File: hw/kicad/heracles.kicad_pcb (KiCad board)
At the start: 2 copper layers, 61 parts, among them J1 USB-MICRO, K1 MOTOR_CONV, P1 LOGIC_BAT, P2 MOTOR_BAT, P3 MOTOR_A, P4 MOTOR_B, P5 CONN_8, P6 CONN_8, P7 CONN_8, P8 CONN_8, P9 CONN_8, Q1 FDV301N, Q2 FDV304P, SW1 B3U-1000P, SW2 B3U-1000P, T1 TPS62056, T2 LM3480, U1 TB6612FNG, U2 HC-05, U3 LY330ALH, U4 MMA6341L, U5 STM32F103CBT6

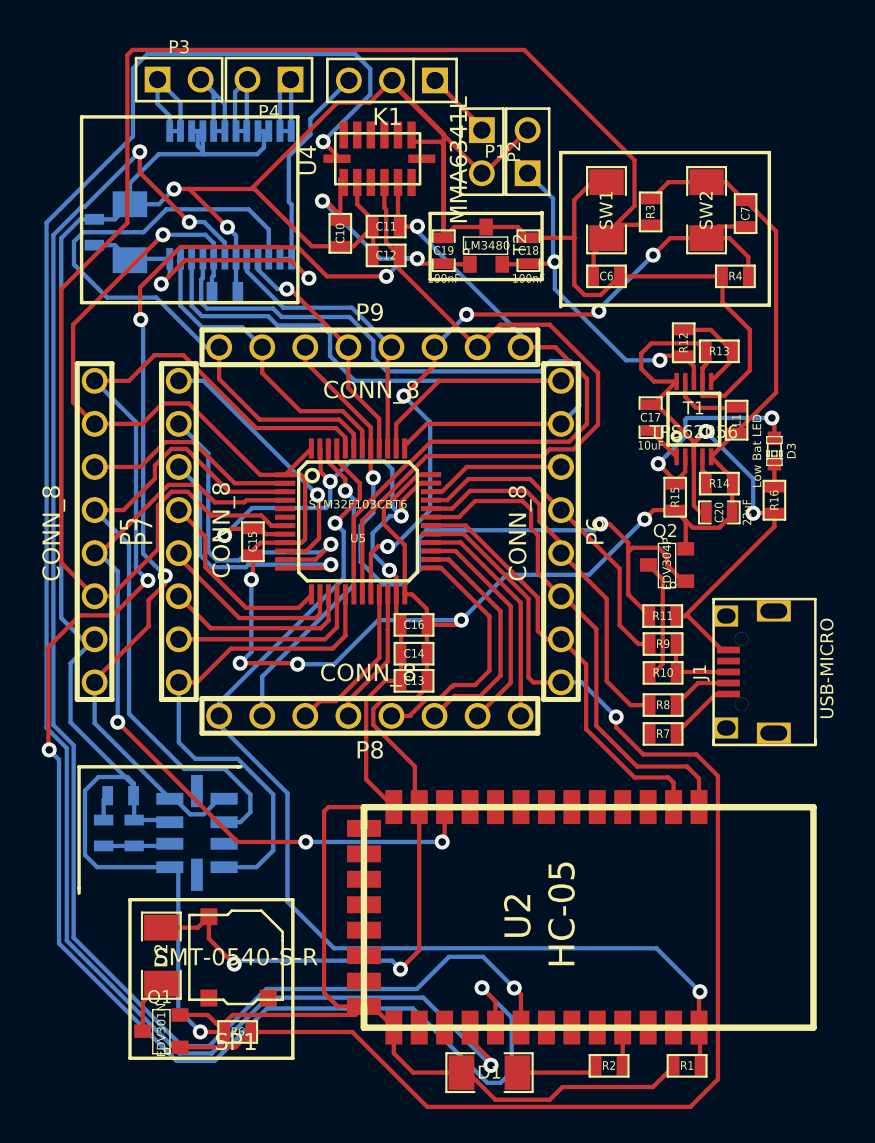
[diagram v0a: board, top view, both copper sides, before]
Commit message: Added some missing connections in pcb
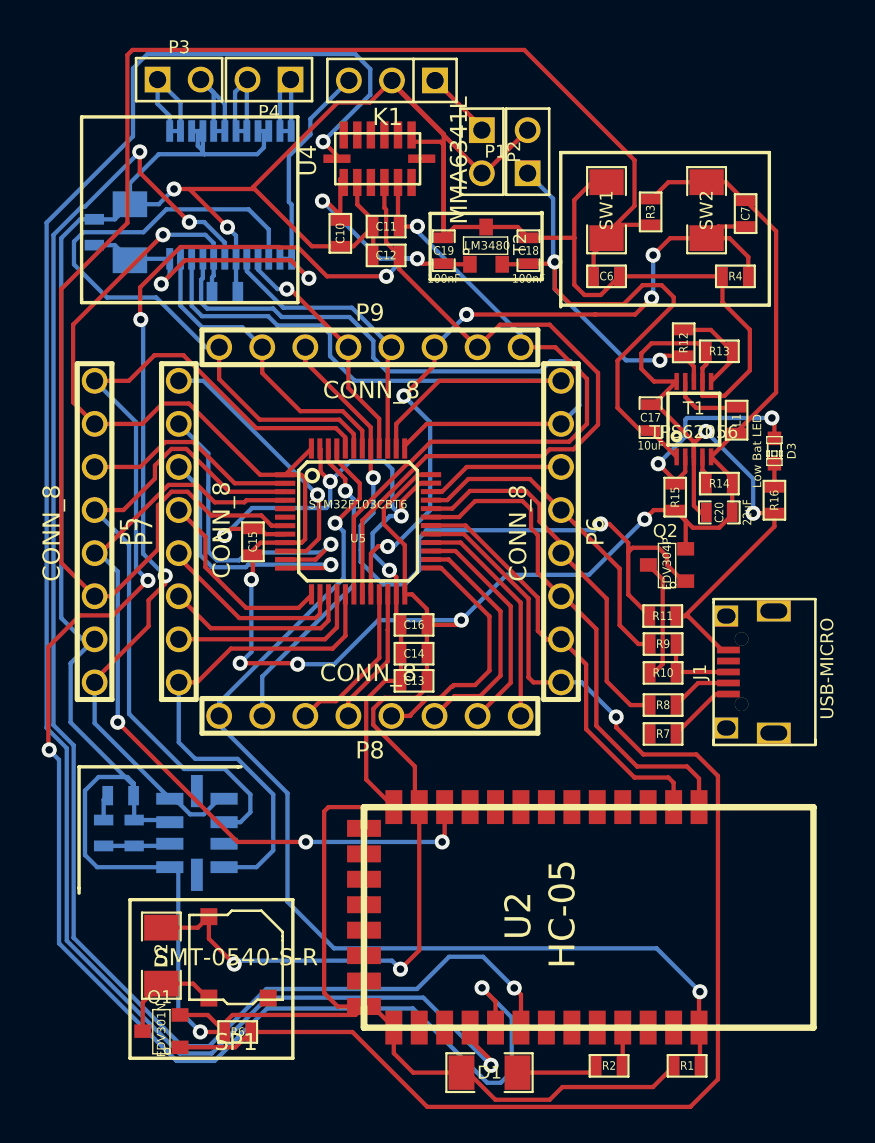
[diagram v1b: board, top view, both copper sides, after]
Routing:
- net /Power/VIN: track 24.4 -> 44.5 mm
- net N-0000086: track 3.25 -> 6.41 mm
- net /Microcontroller/PB2-BOOT1: track 43.4 -> 44.8 mm
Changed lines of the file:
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@@
   (general
     (links 181)
-    (no_connects 2)
+    (no_connects 0)
     (area 195.601 157.2338 243.0625 220.547001)
     (thickness 1.6)
     (drawings 27)
-    (tracks 937)
+    (tracks 953)
     (zones 0)
     (modules 61)
@@
   (segment (start 224.29 190.69) (end 224.29 197.37) (width 0.254) (layer F.Cu) (net 30))
   (segment (start 220.7446 187.1446) (end 224.29 190.69) (width 0.254) (layer F.Cu) (net 30))
+  (segment (start 228.67 173.7) (end 231.04 173.7) (width 0.254) (layer F.Cu) (net 31))
+  (segment (start 233.099 169.201) (end 232.1 170.2) (width 0.254) (layer F.Cu) (net 31))
+  (via (at 232.1 170.2) (size 0.889) (layers F.Cu B.Cu) (net 31))
+  (segment (start 233.099 169.201) (end 235.25 169.201) (width 0.254) (layer F.Cu) (net 31))
+  (segment (start 232.1 172.64) (end 232.1 170.2) (width 0.254) (layer B.Cu) (net 31))
+  (segment (start 232.01 172.73) (end 232.1 172.64) (width 0.254) (layer B.Cu) (net 31))
+  (via (at 232.01 172.73) (size 0.889) (layers F.Cu B.Cu) (net 31))
+  (segment (start 231.04 173.7) (end 232.01 172.73) (width 0.254) (layer F.Cu) (net 31))
   (segment (start 215.89 187.36) (end 216.43 187.36) (width 0.254) (layer F.Cu) (net 31))
   (segment (start 216.84 187.35) (end 218.95 185.24) (width 0.254) (layer B.Cu) (net 31))
@@
   (segment (start 215.9 187.35) (end 215.89 187.36) (width 0.254) (layer F.Cu) (net 31))
   (segment (start 215.89 187.36) (end 215.45692 187.79308) (width 0.254) (layer F.Cu) (net 31))
-  (segment (start 235.25 169.201) (end 233.099 169.201) (width 0.254) (layer F.Cu) (net 31))
   (segment (start 219.21 175.59) (end 219.21 175.63) (width 0.254) (layer B.Cu) (net 31))
   (segment (start 221.1 173.7) (end 219.21 175.59) (width 0.254) (layer B.Cu) (net 31))
   (via (at 221.1 173.7) (size 0.889) (layers F.Cu B.Cu) (net 31))
-  (segment (start 228.7 173.7) (end 221.1 173.7) (width 0.254) (layer F.Cu) (net 31))
-  (segment (start 228.9 173.5) (end 228.7 173.7) (width 0.254) (layer F.Cu) (net 31))
-  (via (at 228.9 173.5) (size 0.889) (layers F.Cu B.Cu) (net 31))
-  (segment (start 228.9 173.4) (end 228.9 173.5) (width 0.254) (layer B.Cu) (net 31))
-  (segment (start 232.1 170.2) (end 228.9 173.4) (width 0.254) (layer B.Cu) (net 31))
-  (via (at 232.1 170.2) (size 0.889) (layers F.Cu B.Cu) (net 31))
-  (segment (start 233.099 169.201) (end 232.1 170.2) (width 0.254) (layer F.Cu) (net 31))
+  (segment (start 228.7 173.7) (end 228.67 173.7) (width 0.254) (layer F.Cu) (net 31))
+  (segment (start 228.67 173.7) (end 221.1 173.7) (width 0.254) (layer F.Cu) (net 31))
   (segment (start 235.25 169.201) (end 236.601 169.201) (width 0.254) (layer F.Cu) (net 31))
-  (segment (start 237.712 170.312) (end 237.712 171.45) (width 0.254) (layer F.Cu) (net 31))
   (segment (start 236.601 169.201) (end 237.712 170.312) (width 0.254) (layer F.Cu) (net 31))
+  (segment (start 237.712 170.312) (end 237.712 171.45) (width 0.254) (layer F.Cu) (net 31))
   (segment (start 237.55 168.512) (end 235.939 168.512) (width 0.254) (layer F.Cu) (net 31))
   (segment (start 235.939 168.512) (end 235.25 169.201) (width 0.254) (layer F.Cu) (net 31))
@@
   (segment (start 235.008 182.878) (end 235.008 182.0925) (width 0.254) (layer F.Cu) (net 49))
   (segment (start 235.238 183.108) (end 235.008 182.878) (width 0.254) (layer F.Cu) (net 49))
+  (segment (start 231.95 180.542) (end 231.342 180.542) (width 0.254) (layer F.Cu) (net 50) (status 400000))
+  (segment (start 226.3 172.18) (end 226.3 170.6) (width 0.254) (layer F.Cu) (net 50))
+  (segment (start 227.21 173.09) (end 226.3 172.18) (width 0.254) (layer F.Cu) (net 50))
+  (segment (start 230.36 173.09) (end 227.21 173.09) (width 0.254) (layer F.Cu) (net 50))
+  (segment (start 231.48 171.97) (end 230.36 173.09) (width 0.254) (layer F.Cu) (net 50))
+  (segment (start 232.6 171.97) (end 231.48 171.97) (width 0.254) (layer F.Cu) (net 50))
+  (segment (start 233.31 172.68) (end 232.6 171.97) (width 0.254) (layer F.Cu) (net 50))
+  (segment (start 233.31 173.11) (end 233.31 172.68) (width 0.254) (layer F.Cu) (net 50))
+  (segment (start 230 176.42) (end 233.31 173.11) (width 0.254) (layer F.Cu) (net 50))
+  (segment (start 230 179.2) (end 230 176.42) (width 0.254) (layer F.Cu) (net 50))
+  (segment (start 231.342 180.542) (end 230 179.2) (width 0.254) (layer F.Cu) (net 50))
   (segment (start 231.95 180.542) (end 231.95 180.5585) (width 0.254) (layer F.Cu) (net 50))
   (segment (start 231.95 180.5585) (end 232.3 180.9085) (width 0.254) (layer F.Cu) (net 50))
   (segment (start 226.3 170.6) (end 226.3 172.2) (width 0.254) (layer B.Cu) (net 50))
-  (segment (start 232.768 176.132) (end 233.9 176.132) (width 0.254) (layer F.Cu) (net 50))
-  (segment (start 232.5 176.4) (end 232.768 176.132) (width 0.254) (layer F.Cu) (net 50))
-  (via (at 232.5 176.4) (size 0.889) (layers F.Cu B.Cu) (net 50))
-  (segment (start 230.5 176.4) (end 232.5 176.4) (width 0.254) (layer B.Cu) (net 50))
   (segment (start 226.3 172.2) (end 230.5 176.4) (width 0.254) (layer B.Cu) (net 50))
+  (segment (start 230.5 176.4) (end 232.5 176.4) (width 0.254) (layer B.Cu) (net 50))
+  (via (at 232.5 176.4) (size 0.889) (layers F.Cu B.Cu) (net 50))
+  (segment (start 232.5 176.4) (end 232.768 176.132) (width 0.254) (layer F.Cu) (net 50))
+  (segment (start 232.768 176.132) (end 233.9 176.132) (width 0.254) (layer F.Cu) (net 50))
   (segment (start 224.75 170.702) (end 226.198 170.702) (width 0.254) (layer F.Cu) (net 50))
+  (segment (start 226.198 170.702) (end 226.3 170.6) (width 0.254) (layer F.Cu) (net 50))
   (segment (start 226.2 166.87) (end 224.7 165.37) (width 0.254) (layer B.Cu) (net 50))
-  (segment (start 226.2 170.5) (end 226.2 166.87) (width 0.254) (layer B.Cu) (net 50))
   (segment (start 226.3 170.6) (end 226.2 170.5) (width 0.254) (layer B.Cu) (net 50))
+  (segment (start 226.2 170.5) (end 226.2 166.87) (width 0.254) (layer B.Cu) (net 50))
   (via (at 226.3 170.6) (size 0.889) (layers F.Cu B.Cu) (net 50))
-  (segment (start 226.198 170.702) (end 226.3 170.6) (width 0.254) (layer F.Cu) (net 50))
   (segment (start 223.2025 170.73982) (end 224.71218 170.73982) (width 0.254) (layer F.Cu) (net 50))
   (segment (start 224.71218 170.73982) (end 224.75 170.702) (width 0.254) (layer F.Cu) (net 50))
@@
   (segment (start 199.7 203.508) (end 199.7 202.308) (width 0.254) (layer B.Cu) (net 58))
   (segment (start 199.7 202.308) (end 199.938 202.07) (width 0.254) (layer B.Cu) (net 58))
+  (segment (start 205.904 214.004) (end 205.824 214.004) (width 0.254) (layer F.Cu) (net 59) (status C00000))
+  (segment (start 204.975 213.155) (end 203.104 213.155) (width 0.254) (layer F.Cu) (net 59) (status 800000))
+  (segment (start 205.824 214.004) (end 204.975 213.155) (width 0.254) (layer F.Cu) (net 59) (status 400000))
   (segment (start 202.00418 215.954) (end 202.00418 214.25482) (width 0.254) (layer F.Cu) (net 59))
   (segment (start 202.00418 214.25482) (end 203.104 213.155) (width 0.254) (layer F.Cu) (net 59))

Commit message: Fixed Q1 and Q2 footprints
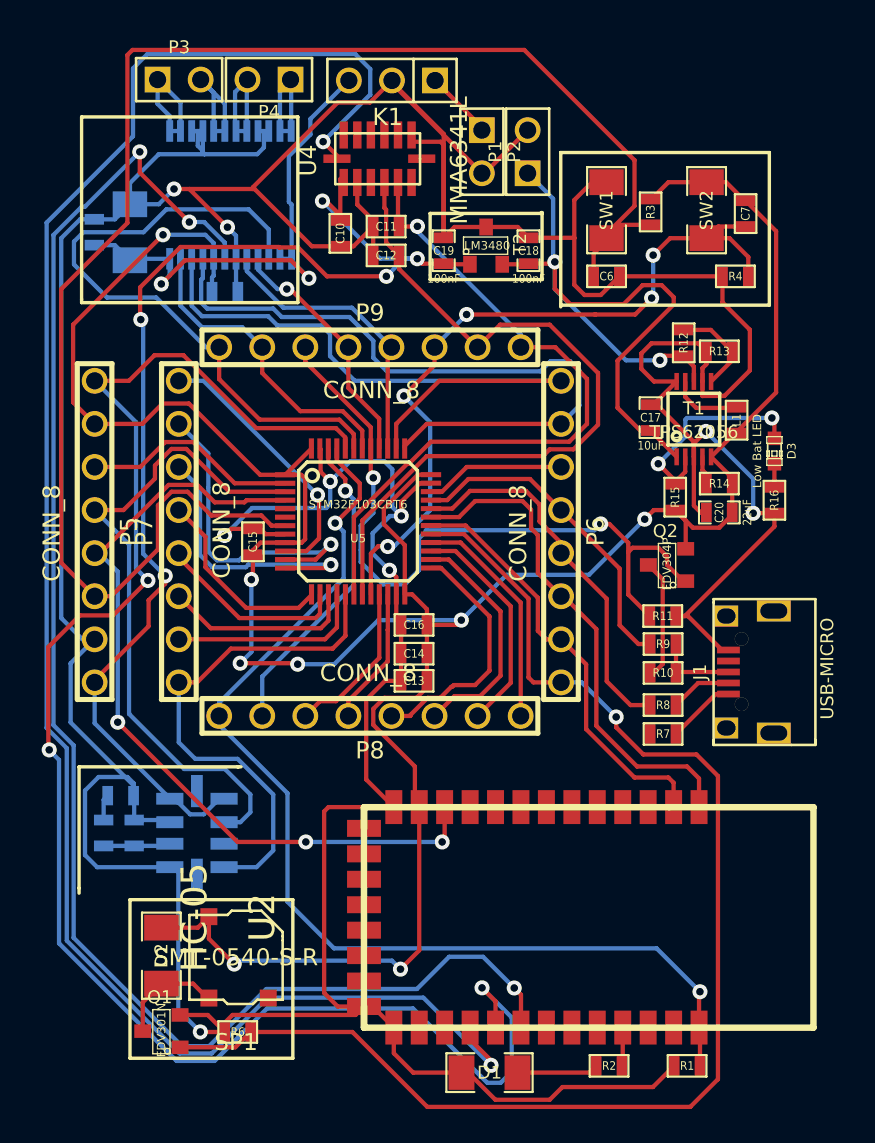
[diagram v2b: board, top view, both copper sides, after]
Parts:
- Q1, Q2: footprint SOT23 -> SOT-23_MOS
